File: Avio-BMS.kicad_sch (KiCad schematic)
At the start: 3 parts, among them J3 5077CR-16SMC2-BK-TR

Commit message: update
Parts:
- added C11: 0.1u, Capacitor_SMD:C_0603_1608Metric_Pad1.08x0.95mm_HandSolder, symbol Device:C_Small
- added C12, C13: 10u, Capacitor_SMD:C_0805_2012Metric_Pad1.18x1.45mm_HandSolder, symbol Device:C_Small
- added D1: LED, LED_THT:LED_D4.0mm, symbol Device:LED
- added J1: +3.3V, Connector_JST:JST_XA_B02B-XASK-1_1x02_P2.50mm_Vertical, symbol Connector_Generic:Conn_01x02
- added J2: +5V, Connector_JST:JST_XA_B02B-XASK-1_1x02_P2.50mm_Vertical, symbol Connector_Generic:Conn_01x02
- added J4: MainBattery, Connector_JST:JST_XA_B02B-XASK-1_1x02_P2.50mm_Vertical, symbol Connector_Generic:Conn_01x02
- added J5: SubBattery, Connector_JST:JST_XA_B02B-XASK-1_1x02_P2.50mm_Vertical, symbol Connector_Generic:Conn_01x02
- added J6, J7, J8: Conn_01x03_Pin, Connector_PinHeader_2.54mm:PinHeader_1x03_P2.54mm_Vertical, symbol Connector:Conn_01x03_Pin
- added L3: 3.3u, symbol Device:L_Small
- added Q1: MBT3906DW1, Package_TO_SOT_SMD:SOT-363_SC-70-6, symbol Transistor_BJT:MBT3906DW1
- added Q2, Q3: Si2333DDS-T1-GE3, Package_TO_SOT_SMD:SOT-23-3, symbol Transistor_FET:Si2319CDS
- added R10, R9: 10k, Resistor_SMD:R_0603_1608Metric_Pad0.98x0.95mm_HandSolder, symbol Device:R_Small
- added R11: 8.2, Resistor_SMD:R_0603_1608Metric_Pad0.98x0.95mm_HandSolder, symbol Device:R_Small
- added R12: 2.94k, Resistor_SMD:R_0603_1608Metric_Pad0.98x0.95mm_HandSolder, symbol Device:R_Small
- added R13: 100k, Resistor_SMD:R_0603_1608Metric_Pad0.98x0.95mm_HandSolder, symbol Device:R_Small
- added R14: 499, Resistor_SMD:R_0603_1608Metric_Pad0.98x0.95mm_HandSolder, symbol Device:R_Small
- added R15: 1k, Resistor_SMD:R_0603_1608Metric_Pad0.98x0.95mm_HandSolder, symbol Device:R_Small
- added TH1: NTC, symbol Device:Thermistor_NTC
- added TP1: VBUS, Connector_Pin:Pin_D1.1mm_L8.5mm_W2.5mm_FlatFork, symbol Connector:TestPoint
- added TP2: BAT-FLOAT4.2V,0.5A, Connector_Pin:Pin_D1.1mm_L8.5mm_W2.5mm_FlatFork, symbol Connector:TestPoint
- added U3: LTC4088EDE-TRPBF, footprints:DFN-14_DE_LIT, symbol 2024-10-02_05-23-37:LTC4088EDE-TRPBF
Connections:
- net GND: now also C11.2, C12.2, C13.2, J1.1 (Pin_1), J2.1 (Pin_1), J4.1 (Pin_1), J5.1 (Pin_1), J6.1 (Pin_1), J7.1 (Pin_1), J8.1 (Pin_1), R10.2, R12.2, R14.2, R9.2, TH1.2, U3.15 (GND)
- net VBUS: now reaches J3.A4_B9 (VBUS), J3.B4_A9 (VBUS)
- net VBUS: now also Q1.1 (E1), Q2.3 (D), TP1.1
- new net: Q1.3 (C2), Q2.1 (G), R10.1
- new net: Q3.1 (G), U3.8 (GATE)
- new net: R11.1, R12.1, U3.2 (CLPROG)
- new net: C11.1, R11.2
- new net: D1.1 (K), R15.1
- new net: Q1.2 (B1), Q1.5 (B2), Q1.6 (C1), R9.1
- new net: L3.1, U3.12 (SW)
- new net: R14.1, U3.5 (C/X), U3.6 (PROG)
- new net *CHRG: R15.2, U3.7 (*CHRG)
- new net +3.3V: J1.2 (Pin_2)
- new net +5V: J2.2 (Pin_2)
- new net D0: J6.2 (Pin_2), U3.13 (D0)
- new net D1: J7.2 (Pin_2), U3.14 (D1)
- new net D2: J8.2 (Pin_2), U3.4 (D2)
- new net Main-Bat: J4.2 (Pin_2), Q3.3 (D), TP2.1, U3.9 (BAT)
- new net NTC: R13.2, TH1.1, U3.1 (NTC)
- new net V_{IN}: C12.1, J6.3 (Pin_3), J7.3 (Pin_3), J8.3 (Pin_3), Q1.4 (E2), Q2.2 (S), R13.1, U3.11 (VBUS)
- new net V_{OUT}1: C13.1, D1.2 (A), L3.2, Q3.2 (S), U3.10 (VOUTS), U3.3 (LDO3V3)
- new net V_{OUT}2: J5.2 (Pin_2)
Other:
- sheet DCDC-3.3V5V renamed DCDC-3.3V,5V
- added sheet PowerPath (PowerPath.kicad_sch)
- note added: "Li-ionバッテリーチャージャー 1cell/PowerPath"
- note added: "PowerPath/MainBat,SubBat"
- note added: "USB-PD"
- moved on the sheet: J3, R7, R8

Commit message: Update KiCad project files
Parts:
- added D2: indi-VBUS, LED_SMD:LED_0603_1608Metric, symbol Device:LED
- added J10, J9: +7.4V, Connector_JST:JST_XA_B02B-XASK-1_1x02_P2.50mm_Vertical, symbol Connector_Generic:Conn_01x02
- added R4: R, Resistor_SMD:R_0603_1608Metric_Pad0.98x0.95mm_HandSolder, symbol Device:R_Small
- D1: value LED -> indi-charge; footprint LED_THT:LED_D4.0mm -> LED_SMD:LED_0603_1608Metric
- J2: value +5V -> +3.3V
- R15: value 1k -> R
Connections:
- net +5V is gone; now on net +3.3V: J2.2 (Pin_2)
- net GND: now also D2.1 (K), J10.1 (Pin_1), J9.1 (Pin_1)
- net VBUS: now also R4.2
- new net: D2.2 (A), R4.1
- new net 7.4V: J10.2 (Pin_2), J9.2 (Pin_2)
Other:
- removed sheet DCDC-3.3V,5V
- removed sheet PowerPath
- added sheet DCDC (DCDC.kicad_sch)
- added sheet LTC4417 (LTC4417.kicad_sch)
- note added: "DCDC3.3V"
- note added: "MainBat-V_{OUT}1,SubBat-V_{OUT}2->VCC"
- note removed: "PowerPath/MainBat,SubBat"
- moved on the sheet: J1, J4, J5

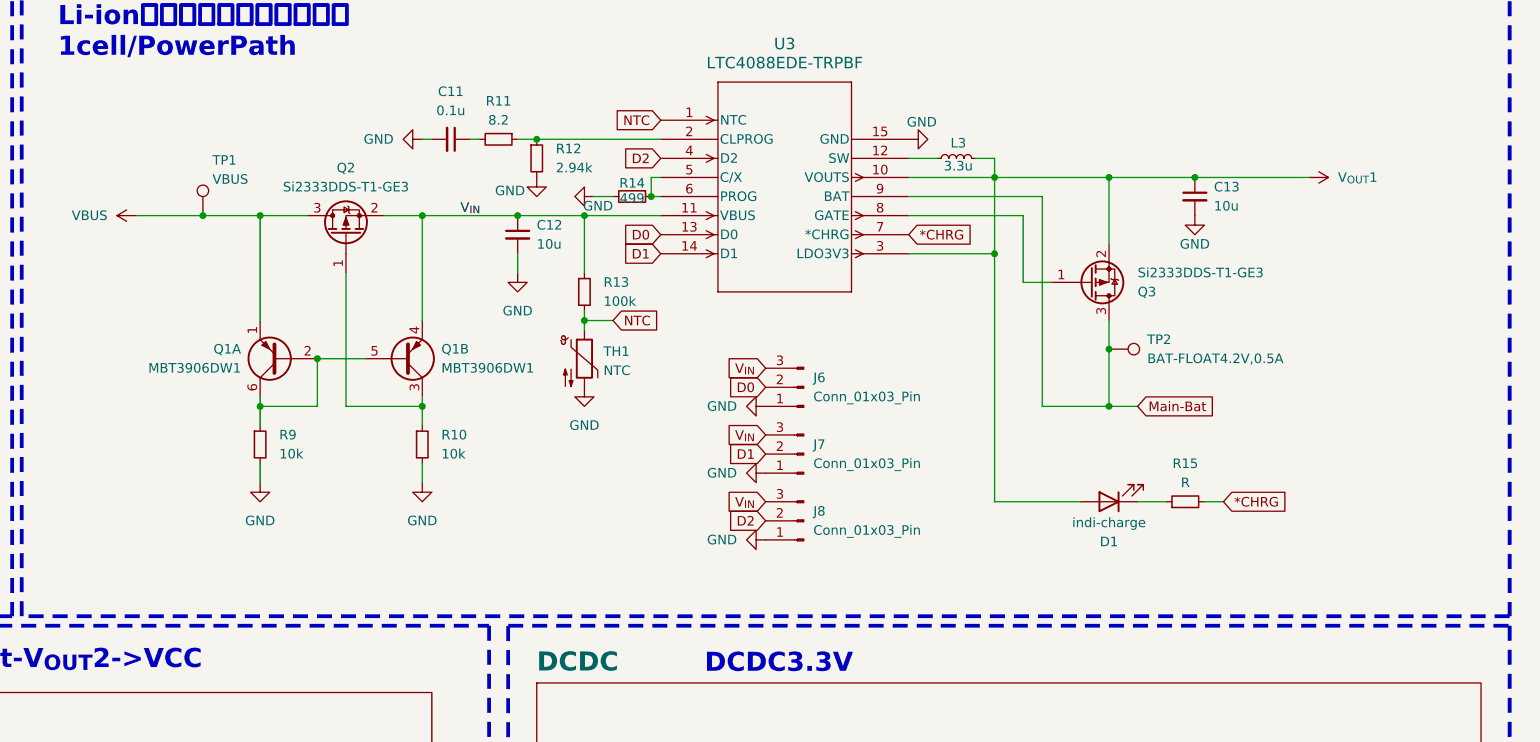
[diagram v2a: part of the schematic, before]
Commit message: LTC4088の修正必須
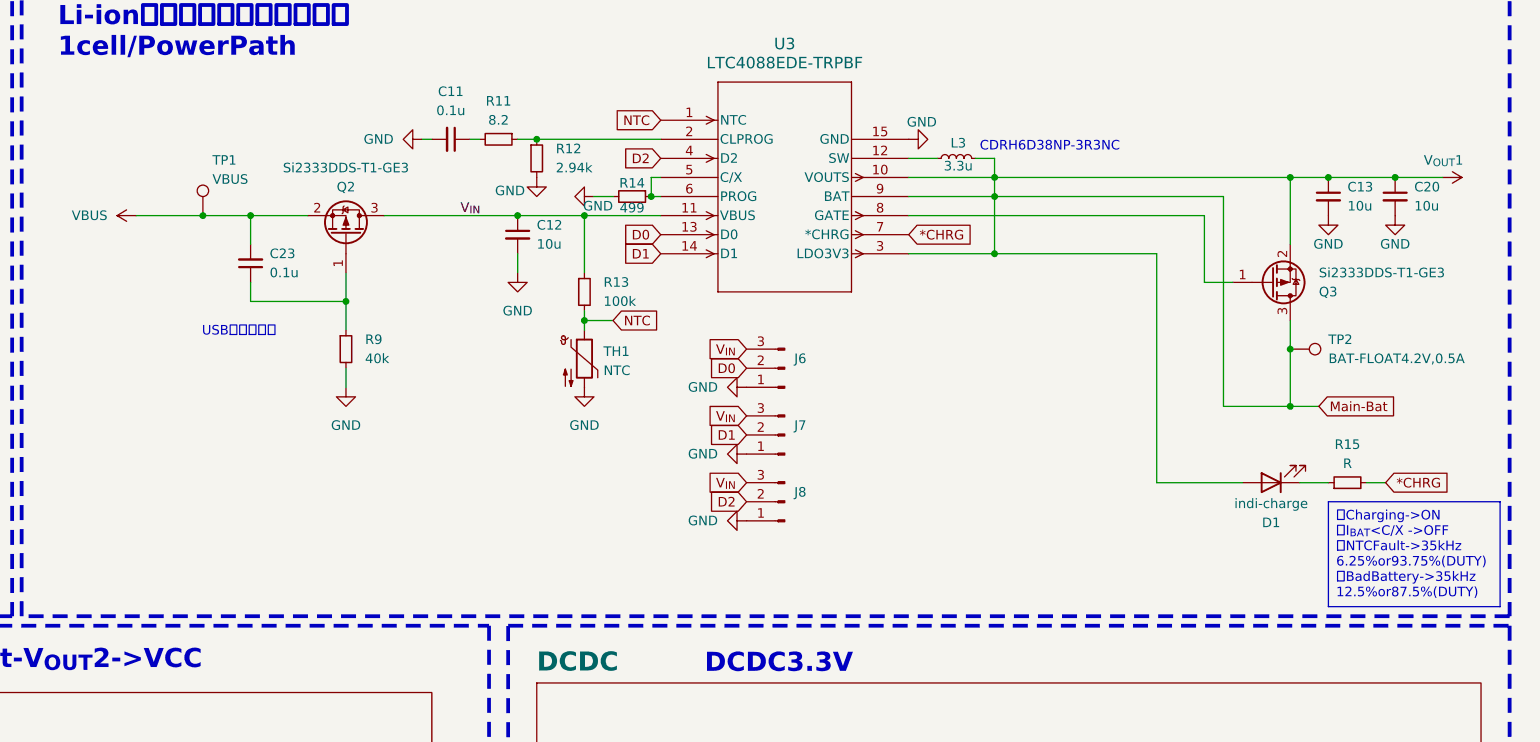
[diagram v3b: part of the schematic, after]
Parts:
- removed Q1: MBT3906DW1, Package_TO_SOT_SMD:SOT-363_SC-70-6, symbol Transistor_BJT:MBT3906DW1
- removed R10: 10k, Resistor_SMD:R_0603_1608Metric_Pad0.98x0.95mm_HandSolder, symbol Device:R_Small
- added C20: 10u, Capacitor_SMD:C_0805_2012Metric_Pad1.18x1.45mm_HandSolder, symbol Device:C_Small
- added C23: 0.1u, Capacitor_SMD:C_0603_1608Metric_Pad1.08x0.95mm_HandSolder, symbol Device:C_Small
- L3: footprint (none) -> CDRH6D38NP-3R3NC:CDRH6D38NP-3R3NC
- R9: value 10k -> 40k
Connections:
- net Main-Bat is gone; now on net V_{OUT}1: J4.2 (Pin_2), Q3.3 (D), TP2.1, U3.9 (BAT)
- net GND: now also C20.2
- net VBUS: now also Q2.2 (S), C23.2; no longer Q2.3 (D)
- net V_{IN}: now also Q2.3 (D); no longer Q2.2 (S)
- net V_{OUT}1: now also C20.1
- net at Q2.1 (G): now also R9.1, C23.1
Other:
- note added: "CDRH6D38NP-3R3NC"
- note added: "USBソフト接続"
- moved on the sheet: C13, D1, J6, J7, J8, Q2, Q3, R15, TP2

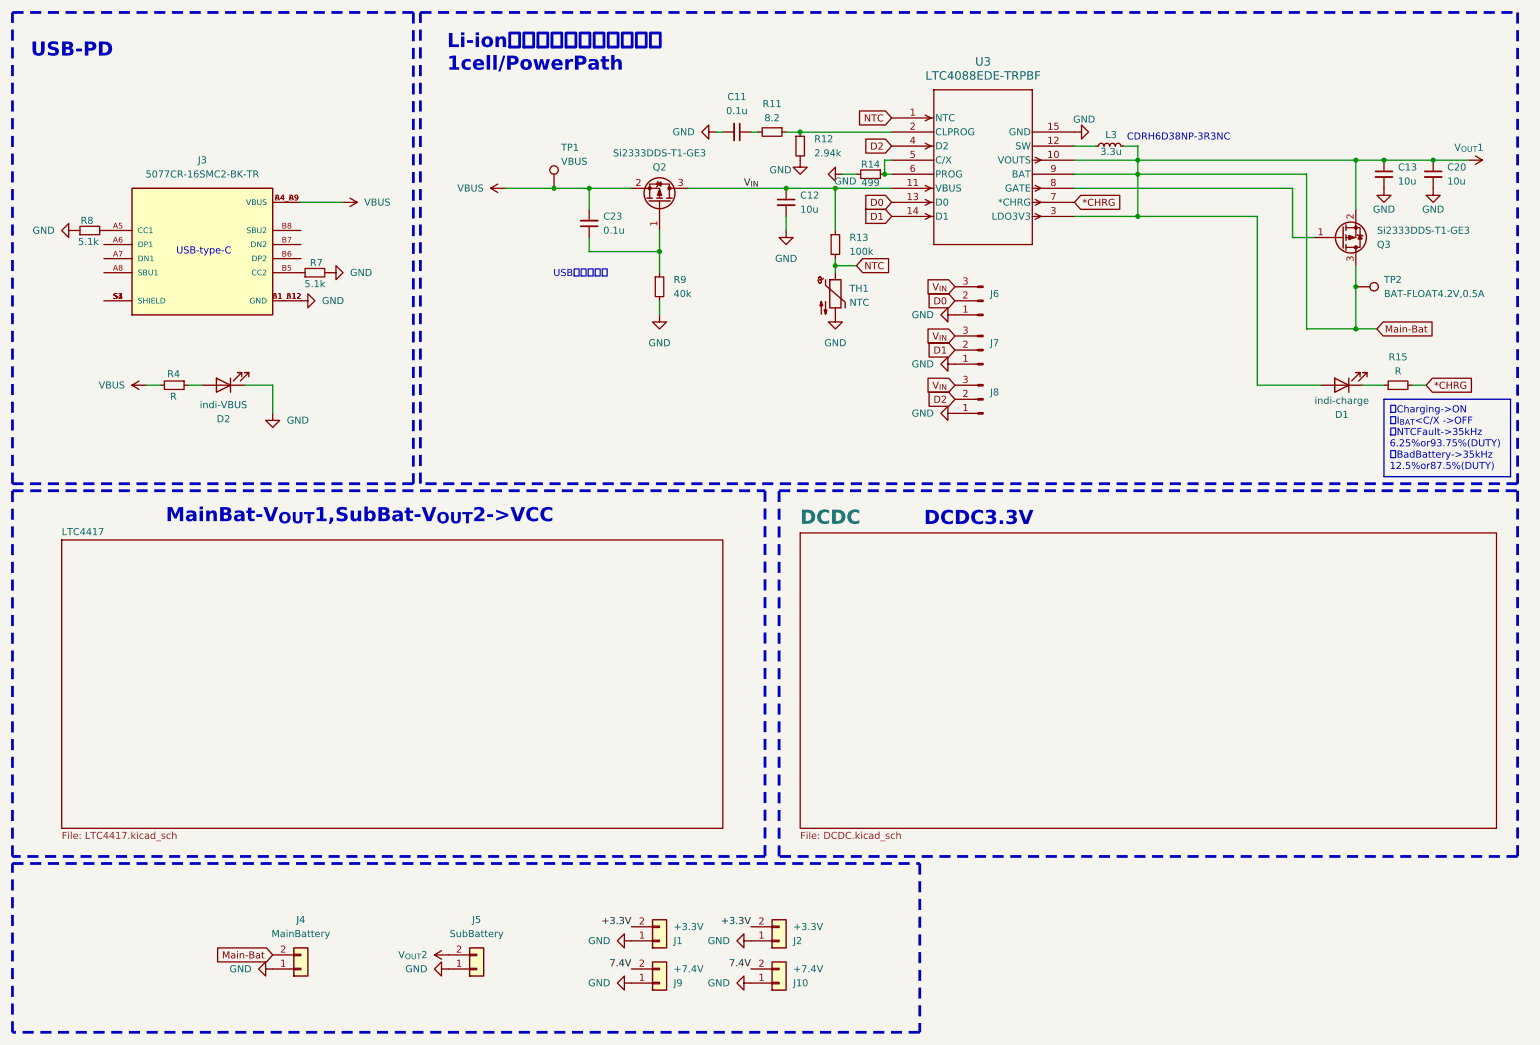
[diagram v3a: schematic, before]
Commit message: add block image
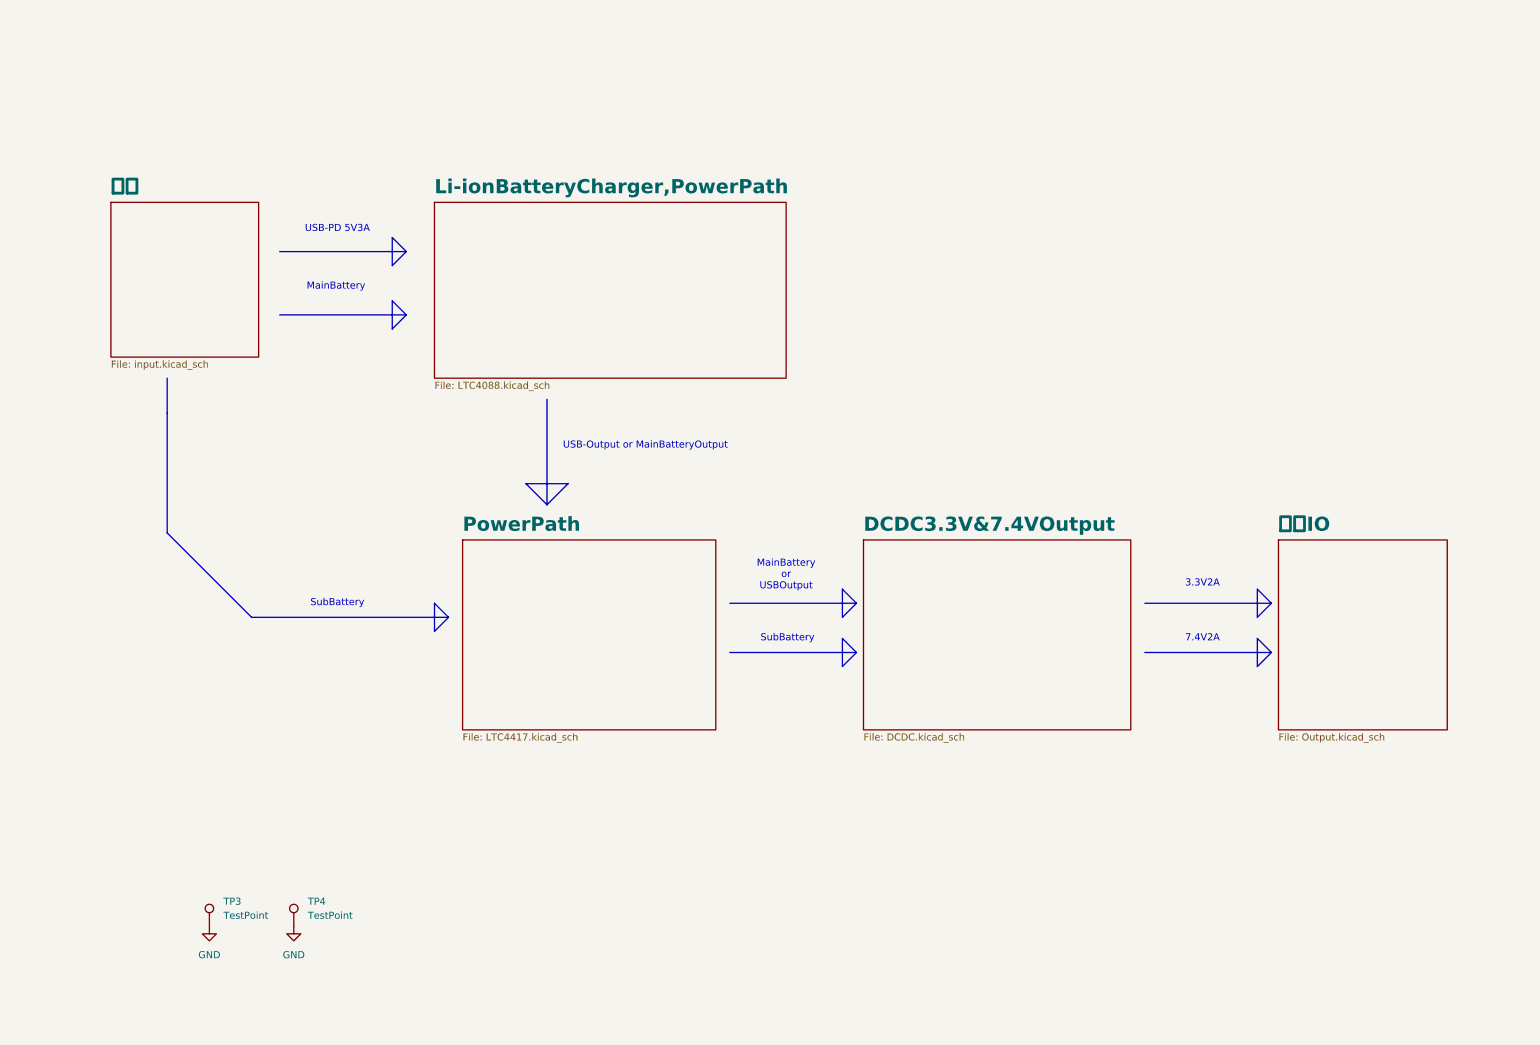
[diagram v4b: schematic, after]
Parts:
- removed C11, C23: 0.1u, Capacitor_SMD:C_0603_1608Metric_Pad1.08x0.95mm_HandSolder, symbol Device:C_Small
- removed C12, C13, C20: 10u, Capacitor_SMD:C_0805_2012Metric_Pad1.18x1.45mm_HandSolder, symbol Device:C_Small
- removed D1: indi-charge, LED_SMD:LED_0603_1608Metric, symbol Device:LED
- removed D2: indi-VBUS, LED_SMD:LED_0603_1608Metric, symbol Device:LED
- removed J1, J2: +3.3V, Connector_JST:JST_XA_B02B-XASK-1_1x02_P2.50mm_Vertical, symbol Connector_Generic:Conn_01x02
- removed J10, J9: +7.4V, Connector_JST:JST_XA_B02B-XASK-1_1x02_P2.50mm_Vertical, symbol Connector_Generic:Conn_01x02
- removed J3: 5077CR-16SMC2-BK-TR, 5077CR-16SMC2-BK-TR:NELTRON_5077CR-16SMC2-BK-TR, symbol 5077CR-16SMC2-BK-TR:5077CR-16SMC2-BK-TR
- removed J4: MainBattery, Connector_JST:JST_XA_B02B-XASK-1_1x02_P2.50mm_Vertical, symbol Connector_Generic:Conn_01x02
- removed J5: SubBattery, Connector_JST:JST_XA_B02B-XASK-1_1x02_P2.50mm_Vertical, symbol Connector_Generic:Conn_01x02
- removed J6, J7, J8: Conn_01x03_Pin, Connector_PinHeader_2.54mm:PinHeader_1x03_P2.54mm_Vertical, symbol Connector:Conn_01x03_Pin
- removed L3: 3.3u, CDRH6D38NP-3R3NC:CDRH6D38NP-3R3NC, symbol Device:L_Small
- removed Q2, Q3: Si2333DDS-T1-GE3, Package_TO_SOT_SMD:SOT-23-3, symbol Transistor_FET:Si2319CDS
- removed R11: 8.2, Resistor_SMD:R_0603_1608Metric_Pad0.98x0.95mm_HandSolder, symbol Device:R_Small
- removed R12: 2.94k, Resistor_SMD:R_0603_1608Metric_Pad0.98x0.95mm_HandSolder, symbol Device:R_Small
- removed R13: 100k, Resistor_SMD:R_0603_1608Metric_Pad0.98x0.95mm_HandSolder, symbol Device:R_Small
- removed R14: 499, Resistor_SMD:R_0603_1608Metric_Pad0.98x0.95mm_HandSolder, symbol Device:R_Small
- removed R15, R4: R, Resistor_SMD:R_0603_1608Metric_Pad0.98x0.95mm_HandSolder, symbol Device:R_Small
- removed R7, R8: 5.1k, Resistor_SMD:R_0603_1608Metric_Pad0.98x0.95mm_HandSolder, symbol Device:R_Small
- removed R9: 40k, Resistor_SMD:R_0603_1608Metric_Pad0.98x0.95mm_HandSolder, symbol Device:R_Small
- removed TH1: NTC, symbol Device:Thermistor_NTC
- removed TP1: VBUS, Connector_Pin:Pin_D1.1mm_L8.5mm_W2.5mm_FlatFork, symbol Connector:TestPoint
- removed TP2: BAT-FLOAT4.2V,0.5A, Connector_Pin:Pin_D1.1mm_L8.5mm_W2.5mm_FlatFork, symbol Connector:TestPoint
- removed U3: LTC4088EDE-TRPBF, footprints:DFN-14_DE_LIT, symbol 2024-10-02_05-23-37:LTC4088EDE-TRPBF
- added TP3, TP4: TestPoint, Connector_PinHeader_2.54mm:PinHeader_1x01_P2.54mm_Vertical, symbol Connector:TestPoint
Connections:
- net GND: now also TP3.1, TP4.1
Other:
- sheet DCDC renamed DCDC3.3V&7.4VOutput
- sheet LTC4417 renamed PowerPath
- added sheet Li-ionBatteryCharger,PowerPath (LTC4088.kicad_sch)
- added sheet 入力 (input.kicad_sch)
- added sheet 出力IO (Output.kicad_sch)
- note added: "3.3V2A"
- note added: "7.4V2A"
- note added: "MainBattery"
- note added: "MainBattery or USBOutput"
- note added: "SubBattery"
- note added: "USB-Output or MainBatteryOutput"
- note added: "USB-PD 5V3A"
- note removed: "CDRH6D38NP-3R3NC"
- note removed: "DCDC3.3V"
- note removed: "Li-ionバッテリーチャージャー 1cell/PowerPath"
- note removed: "MainBat-V_{OUT}1,SubBat-V_{OUT}2->VCC"
- note removed: "USB-PD"
- note removed: "USB-type-C"
- note removed: "USBソフト接続"

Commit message: update pcb
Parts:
- renumbered TP3 to TP1, TP4 to TP2
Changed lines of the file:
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@@
 		(dnp no)
 		(fields_autoplaced yes)
-		(property "Reference" "TP3"
+		(property "Reference" "TP1"
 			(at 50.8 173.2279 0)
 			(effects
@@
 			(project ""
 				(path "/14e0994b-afc2-4c10-b50d-3efcc006980d"
-					(reference "TP3")
+					(reference "TP1")
 					(unit 1)
 				)
@@
 		(dnp no)
 		(fields_autoplaced yes)
-		(property "Reference" "#PWR055"
+		(property "Reference" "#PWR02"
 			(at 63.5 184.15 0)
 			(effects
@@
 			(project "Avio-BMS"
 				(path "/14e0994b-afc2-4c10-b50d-3efcc006980d"
-					(reference "#PWR055")
+					(reference "#PWR02")
 					(unit 1)
 				)
@@
 		(dnp no)
 		(fields_autoplaced yes)
-		(property "Reference" "#PWR054"
+		(property "Reference" "#PWR01"
 			(at 48.26 184.15 0)
 			(effects
@@
 			(project ""
 				(path "/14e0994b-afc2-4c10-b50d-3efcc006980d"
-					(reference "#PWR054")
+					(reference "#PWR01")
 					(unit 1)
 				)
@@
 		(dnp no)
 		(fields_autoplaced yes)
-		(property "Reference" "TP4"
+		(property "Reference" "TP2"
 			(at 66.04 173.2279 0)
 			(effects
@@
 			(project "Avio-BMS"
 				(path "/14e0994b-afc2-4c10-b50d-3efcc006980d"
-					(reference "TP4")
-					(unit 1)
-				)
+					(reference "TP2")
+					(unit 1)
+				)

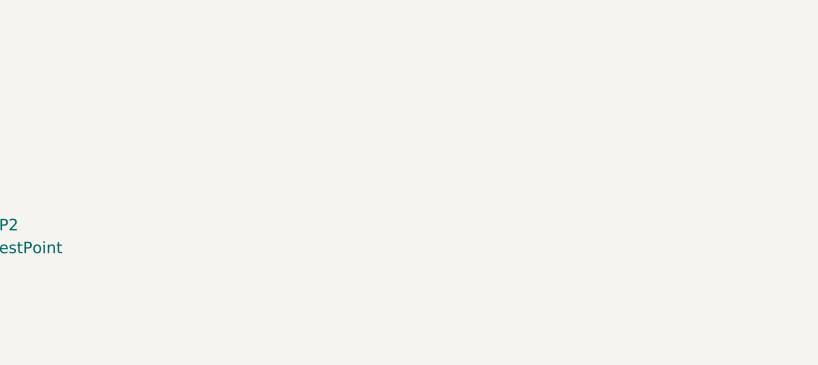
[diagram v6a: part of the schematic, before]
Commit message: remove autosave and lock files; update component values and footprints; add new drill and Gerber files; create BOM
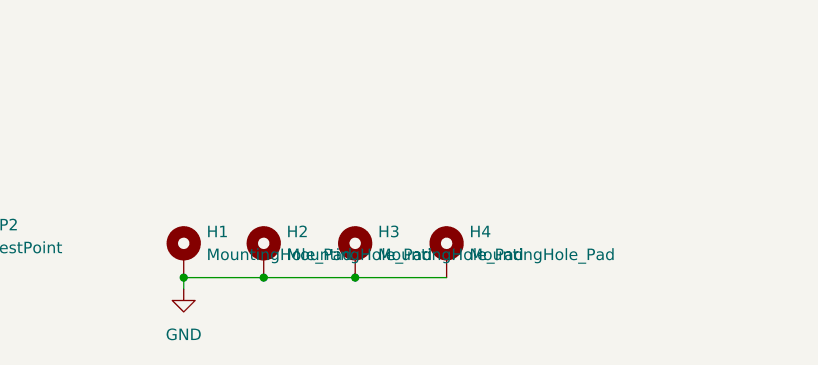
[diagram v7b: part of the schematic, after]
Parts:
- added H1, H2, H3, H4: MountingHole_Pad, MountingHole:MountingHole_3.2mm_M3_Pad_Via, symbol Mechanical:MountingHole_Pad
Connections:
- net GND: now also H1.1, H2.1, H3.1, H4.1
